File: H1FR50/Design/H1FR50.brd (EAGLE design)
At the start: 34.6 x 30 mm, 49 parts, among them P1 HEXABIT_17.32_NO_P6, U1 STM32F091CBU6, U2 TPS22943DCKR, U3 BGA824N6, U4 TESEO-LIV3F, U5 B39162B4327P810, X1 XTALL_CSTCE8M00G52

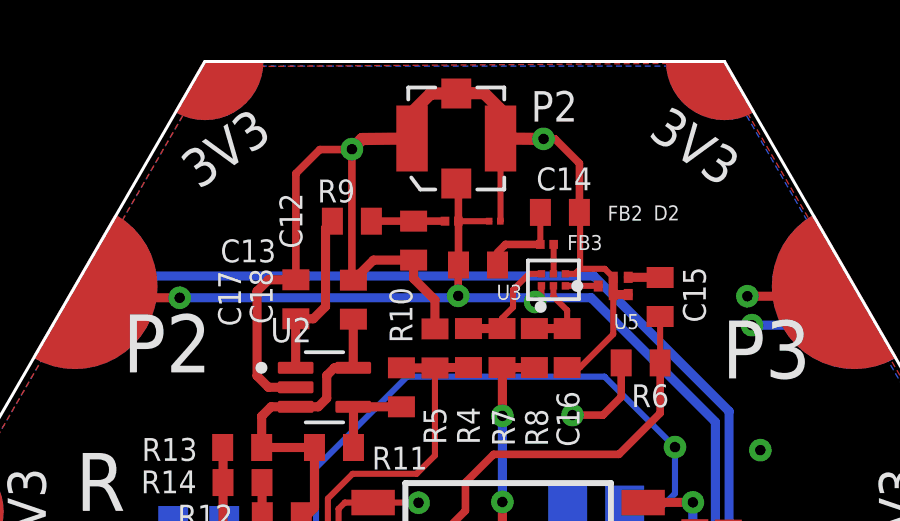
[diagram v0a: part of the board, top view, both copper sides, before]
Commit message: Added Keepout areas in PCB..
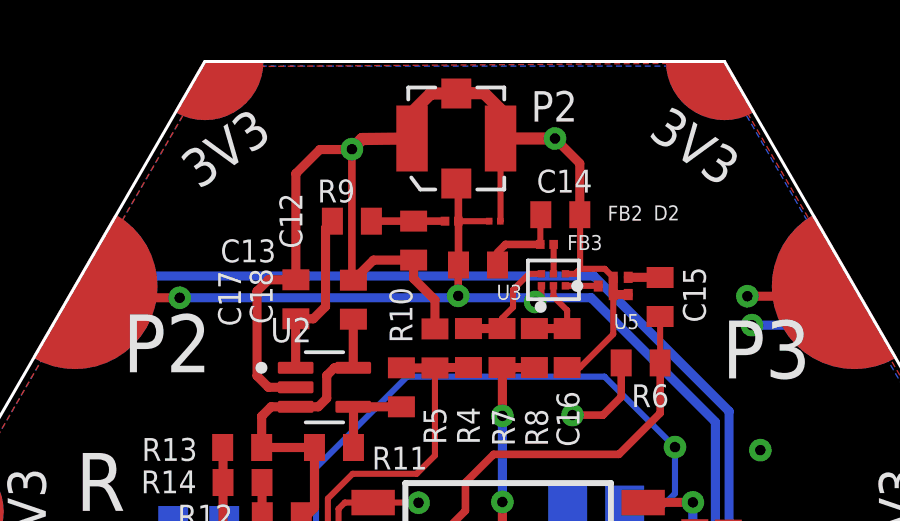
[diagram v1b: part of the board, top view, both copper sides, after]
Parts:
- moved C14 0.08 mm to (3.19, 9.89)
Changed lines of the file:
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@@
 <drawing>
 <settings>
-<setting alwaysvectorfont="no"/>
+<setting alwaysvectorfont="yes"/>
 <setting verticaltext="up"/>
 </settings>
@@
 <layer number="132" name="bAdjust" color="7" fill="1" visible="yes" active="yes"/>
 <layer number="133" name="bottom_silk" color="7" fill="1" visible="yes" active="yes"/>
+<layer number="134" name="cKeepout" color="16" fill="10" visible="yes" active="yes"/>
+<layer number="135" name="dKeepout" color="23" fill="10" visible="yes" active="yes"/>
 <layer number="144" name="Drill_legend" color="7" fill="1" visible="yes" active="yes"/>
 <layer number="145" name="DrillLegend_01-02" color="7" fill="1" visible="yes" active="yes"/>
@@
 <rectangle x1="-6.37920625" y1="-6.89889375" x2="-6.29081875" y2="-6.8841625" layer="21" rot="R180"/>
 <text x="3.6957" y="-12.5984" size="1.778" layer="25">D</text>
+<rectangle x1="-2.7178" y1="10.414" x2="2.3241" y2="14.6685" layer="39"/>
+<rectangle x1="-2.7178" y1="10.414" x2="2.3241" y2="14.6685" layer="40"/>
+<rectangle x1="-2.7178" y1="10.414" x2="2.3241" y2="14.6685" layer="135"/>
+<rectangle x1="-2.7178" y1="10.414" x2="2.3241" y2="14.6685" layer="134"/>
 </plain>
 <attributes>
@@
 <attribute name="VOLTAGE_RATING" value="" x="-21.2598" y="6.8199" size="1.778" layer="27" display="off"/>
 </element>
-<element name="C14" library="HEXABITZ_RCLS" library_urn="urn:adsk.eagle:library:20064561" package="C-0402" package3d_urn="urn:adsk.eagle:package:19666459/2" value="3.9pF" x="3.175" y="9.9695" smashed="yes" rot="R180">
-<attribute name="CAPACITANCE" value="" x="35.5727" y="15.8877" size="1.778" layer="27" rot="R180" display="off"/>
-<attribute name="MFN" value="" x="35.5727" y="15.8877" size="1.778" layer="27" rot="R180" display="off"/>
-<attribute name="MPN" value="" x="35.5727" y="15.8877" size="1.778" layer="27" rot="R180" display="off"/>
-<attribute name="NAME" x="2.3876" y="10.7061" size="0.762" layer="25"/>
-<attribute name="OCTOPART_URL" value="" x="35.5727" y="15.8877" size="1.778" layer="27" rot="R180" display="off"/>
-<attribute name="TOLERANCE" value="" x="35.5727" y="15.8877" size="1.778" layer="27" rot="R180" display="off"/>
-<attribute name="VALUE" x="3.81" y="11.8745" size="1.016" layer="27" rot="R180"/>
-<attribute name="VOLTAGE_RATING" value="" x="35.5727" y="15.8877" size="1.778" layer="27" rot="R180" display="off"/>
+<element name="C14" library="HEXABITZ_RCLS" library_urn="urn:adsk.eagle:library:20064561" package="C-0402" package3d_urn="urn:adsk.eagle:package:19666459/2" value="3.9pF" x="3.1877" y="9.8933" smashed="yes" rot="R180">
+<attribute name="CAPACITANCE" value="" x="35.5854" y="15.8115" size="1.778" layer="27" rot="R180" display="off"/>
+<attribute name="MFN" value="" x="35.5854" y="15.8115" size="1.778" layer="27" rot="R180" display="off"/>
+<attribute name="MPN" value="" x="35.5854" y="15.8115" size="1.778" layer="27" rot="R180" display="off"/>
+<attribute name="NAME" x="2.4003" y="10.6299" size="0.762" layer="25"/>
+<attribute name="OCTOPART_URL" value="" x="35.5854" y="15.8115" size="1.778" layer="27" rot="R180" display="off"/>
+<attribute name="TOLERANCE" value="" x="35.5854" y="15.8115" size="1.778" layer="27" rot="R180" display="off"/>
+<attribute name="VALUE" x="3.8227" y="11.7983" size="1.016" layer="27" rot="R180"/>
+<attribute name="VOLTAGE_RATING" value="" x="35.5854" y="15.8115" size="1.778" layer="27" rot="R180" display="off"/>
 </element>
 <element name="FB3" library="HEXABITZ_RCLS" library_urn="urn:adsk.eagle:library:20064561" package="FB-0402" package3d_urn="urn:adsk.eagle:package:27264799/1" value="6.8nH" x="2.7432" y="8.9027" smashed="yes">
@@
 <wire x1="-3.7592" y1="12.0777" x2="-3.420453125" y2="12.416446875" width="0.4064" layer="1"/>
 <via x="-3.7592" y="12.0777" extent="1-2" drill="0.35"/>
-<wire x1="2.6289" y1="12.4206" x2="2.62711875" y2="12.41881875" width="0.3048" layer="1"/>
-<wire x1="2.62711875" y1="12.41881875" x2="1.1956" y2="12.4333" width="0.4064" layer="1"/>
-<via x="2.6289" y="12.4206" extent="1-2" drill="0.35"/>
+<via x="3.0099" y="12.4333" extent="1-2" drill="0.35"/>
 <wire x1="3.3591" y1="7.9216" x2="3.6798" y2="7.9216" width="0.2032" layer="1"/>
 <wire x1="3.6798" y1="7.9216" x2="3.8481" y2="8.0899" width="0.2032" layer="1"/>
-<wire x1="3.8481" y1="8.0899" x2="3.8481" y2="9.9464" width="0.2032" layer="1"/>
-<wire x1="3.8481" y1="9.9464" x2="3.825" y2="9.9695" width="0.3048" layer="1"/>
+<wire x1="3.8481" y1="8.0899" x2="3.8481" y2="9.8829" width="0.2032" layer="1"/>
+<wire x1="3.8481" y1="9.8829" x2="3.8377" y2="9.8933" width="0.3048" layer="1"/>
 <wire x1="2.5591" y1="7.5216" x2="2.5591" y2="7.1946" width="0.2032" layer="1"/>
 <wire x1="2.5591" y1="7.1946" x2="2.3495" y2="6.985" width="0.2032" layer="1"/>
@@
 <wire x1="-2.3262" y1="-11.0638" x2="-2.7051" y2="-11.4427" width="0.2032" layer="16"/>
 <wire x1="-2.3262" y1="-11.0638" x2="-2.3262" y2="-10.51120625" width="0.2032" layer="16"/>
-<wire x1="3.825" y1="9.9695" x2="3.825" y2="11.6055" width="0.254" layer="1"/>
-<wire x1="3.825" y1="11.6055" x2="3.0099" y2="12.4206" width="0.254" layer="1"/>
-<wire x1="3.0099" y1="12.4206" x2="2.6289" y2="12.4206" width="0.254" layer="1"/>
-<wire x1="-5.6261" y1="7.7239" x2="-5.6261" y2="11.2649" width="0.254" layer="1"/>
-<wire x1="-4.826" y1="12.065" x2="-3.7592" y2="12.065" width="0.254" layer="1"/>
-<wire x1="-5.6261" y1="11.2649" x2="-4.826" y2="12.065" width="0.254" layer="1"/>
+<wire x1="3.8377" y1="9.8933" x2="3.8377" y2="11.5928" width="0.3048" layer="1"/>
+<wire x1="-5.6261" y1="7.7239" x2="-5.6261" y2="11.2649" width="0.3048" layer="1"/>
+<wire x1="-4.826" y1="12.065" x2="-3.7592" y2="12.065" width="0.3048" layer="1"/>
+<wire x1="-5.6261" y1="11.2649" x2="-4.826" y2="12.065" width="0.3048" layer="1"/>
 <wire x1="-3.8236" y1="-11.2513" x2="-4.7235" y2="-10.3514" width="0.2032" layer="1"/>
 <wire x1="-4.7235" y1="-10.3514" x2="-5.1435" y2="-10.3514" width="0.2032" layer="1"/>
@@
 <wire x1="-1.5425" y1="0.2979" x2="-1.5367" y2="0.2921" width="0.2032" layer="1"/>
 <via x="-1.5367" y="0.2921" extent="1-2" drill="0.35"/>
+<wire x1="1.1956" y1="12.4333" x2="3.0099" y2="12.4333" width="0.4064" layer="1"/>
+<wire x1="3.8377" y1="11.5928" x2="3.8377" y2="11.6055" width="0.2032" layer="1"/>
+<wire x1="3.8377" y1="11.6055" x2="3.0099" y2="12.4333" width="0.3048" layer="1"/>
 </signal>
 <signal name="VDD">
@@
 <contactref element="FB3" pad="1"/>
 <contactref element="C14" pad="2"/>
-<wire x1="2.5212" y1="9.9657" x2="2.525" y2="9.9695" width="0.3048" layer="1"/>
+<wire x1="2.5212" y1="9.8768" x2="2.5377" y2="9.8933" width="0.3048" layer="1"/>
 <wire x1="2.5212" y1="8.9027" x2="1.3612" y2="8.9027" width="0.254" layer="1"/>
 <wire x1="1.3612" y1="8.9027" x2="1.0945" y2="8.636" width="0.254" layer="1"/>
 <wire x1="1.0945" y1="8.636" x2="1.0945" y2="8.2169" width="0.2032" layer="1"/>
-<wire x1="2.5212" y1="8.9027" x2="2.5212" y2="9.9657" width="0.2032" layer="1"/>
+<wire x1="2.5212" y1="8.9027" x2="2.5212" y2="9.8768" width="0.2032" layer="1"/>
 </signal>
 <signal name="N$12">

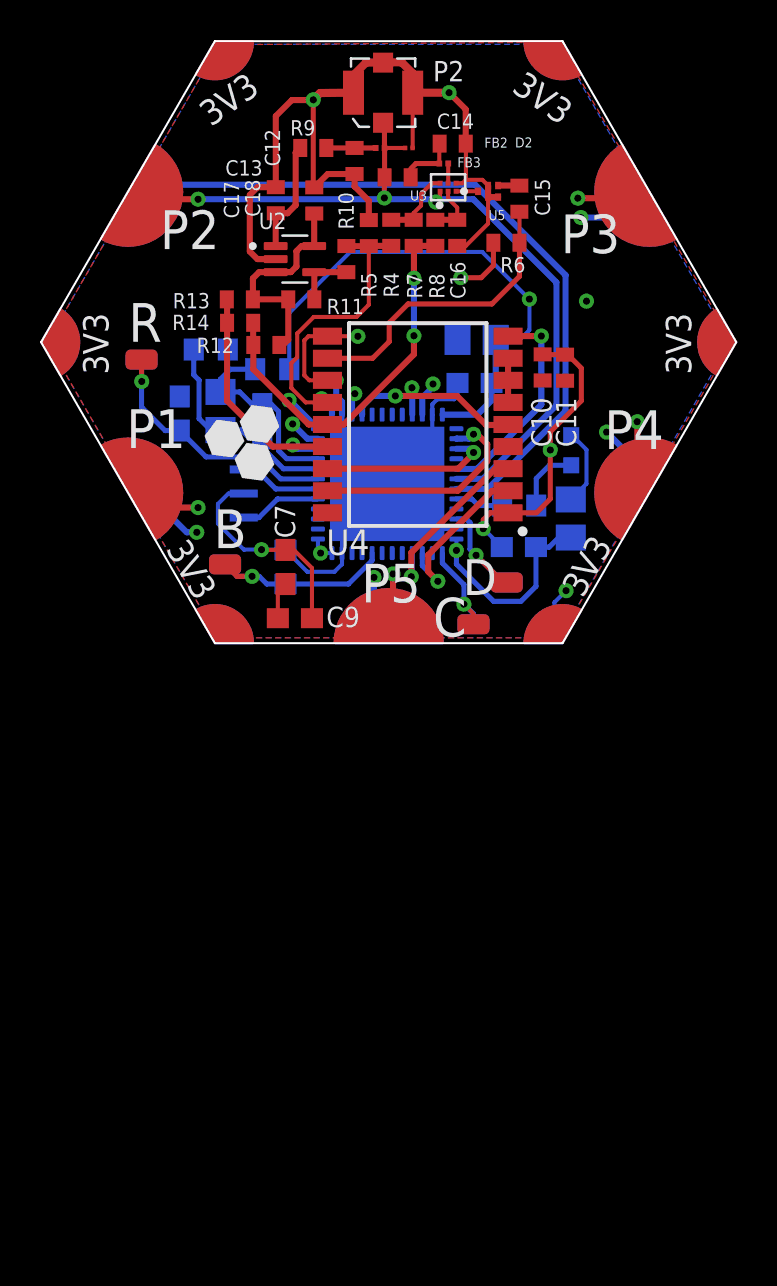
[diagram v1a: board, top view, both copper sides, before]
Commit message: - Rearanged all P#.. - Removed Keepout areas.. - Renamed all NM to DNP.. - Moved D1 from layer 16 to layer 1.. - Changed R8 from 0R NM to 0R.. - Placed more Grounding vias around RF connector in brd.. - Added two pullups res on I2C lines.. - Added the recomended filters on Tevo's power pins.. - Updated Document.. - Updated BOM..
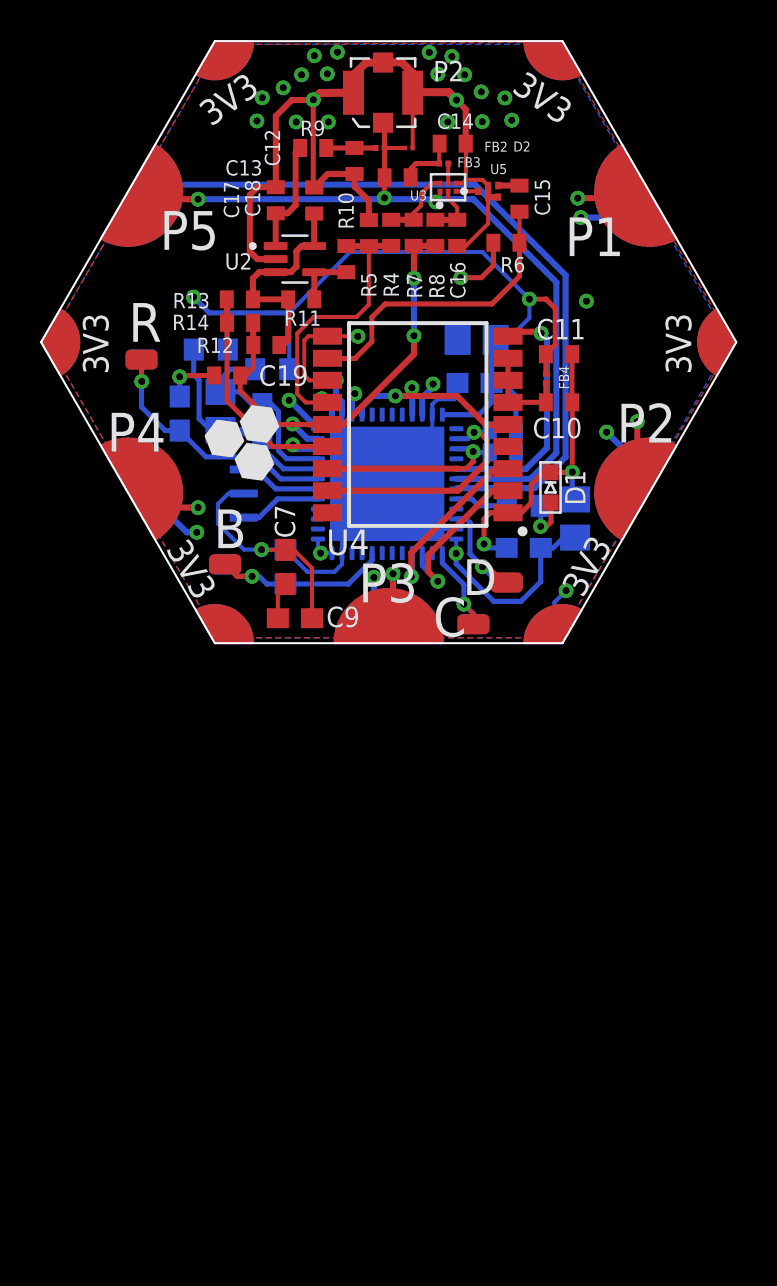
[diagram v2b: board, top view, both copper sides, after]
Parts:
- added C19: 56pF, HEXABITZ_RCLS:C-0402
- added FB4: 27nH, HEXABITZ_RCLS:FB-0402
- added R15, R16: 2.2k, HEXABITZ_RCLS:R-0402
- C10: value 100pF -> 56pF
- C11: value 100nF -> 10nF
- R11, R13, R6, R7, R9: value 0.0R NM -> DNP
- R14: value 3R NM -> DNP
- R8: value 0.0R NM -> 0.0R
- moved D1 2.12 mm to (8.06, -7.24), flipped to the top
- moved C10 1.92 mm to (8.48, -3.00), turned to 180 degrees
- moved C11 0.74 mm to (8.48, -0.60), turned to 180 degrees
- moved C6 0.24 mm to (6.73, -10.2)
- moved R1 0.23 mm to (6.73, -8.15)
- moved C3 0.22 mm to (9.29, -8.79)
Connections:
- new net VCC_RF1: C10.2, FB4.1, U4.6, U4.7, U4.8
- net GND: now also C10.1, C11.1, C19.1; no longer C10.2, C11.2
- net I2C_CLOCK: now also R15.2
- net I2C_DATA: now also R16.2
- net VCC_RF: now also C19.2
- net VDD: now also C11.2, FB4.2, R15.1, R16.1; no longer C10.1, C11.1, U4.6, U4.7, U4.8
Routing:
- net VDD: track 41.8 -> 53.7 mm, vias 3 -> 4
- net VCC_RF1: track 0.00 -> 5.06 mm
- net SYS_RESET: track 10.6 -> 12.6 mm
- net VCC_RF: track 19.4 -> 21.1 mm
- net USART1_TX: track 35.1 -> 36.5 mm
- net USART1_RX: track 37.2 -> 38.5 mm
- net I2C_DATA: track 8.57 -> 9.64 mm
- net I2C_CLOCK: track 11.3 -> 12.3 mm
- net N$10: track 3.36 -> 2.64 mm, vias 0 -> 1
- net GND: track 103.5 -> 103.2 mm, vias 8 -> 9

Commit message: - Redesigned both Schematic and PCB.. - Updated BOM and Documentation..
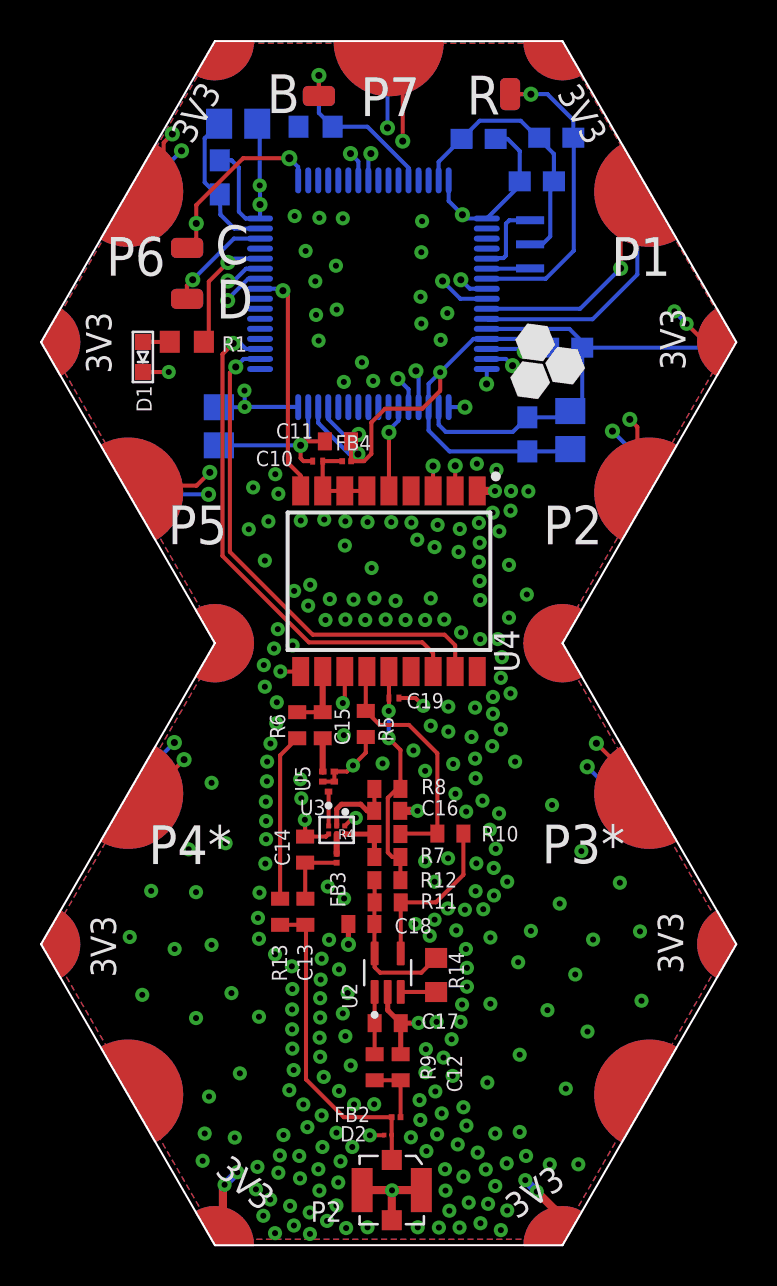
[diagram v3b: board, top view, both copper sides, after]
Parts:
- removed FB1: FB-TDK_MMZ1608Y300B, Hexabitz:FB-TDK_MMZ1608Y300B
- removed R15, R16: 2.2k, HEXABITZ_RCLS:R-0402
- removed R3: 0.0R, Hexabitz:R-0603
- C1: value 100nF -> 10nF
- C10, C19: device HEXABITZ_RCLS:C-0402 -> HEXABITZ_RCLS:C-0201
- C17: value 1uF -> 1.00uF
- C3: value 4.7uF -> 100nF; device Hexabitz:C-0805-POL -> Hexabitz:C-0603
- C5: value 10nF -> 100nF
- C7: value 100nF -> 4.7uF; device Hexabitz:C-0603 -> Hexabitz:C-0805-POL
- P1: value HEXABIT_17.32_NO_P6 -> HEXABIT_17.32_X2_NO_P5; device hexabitz_connectors:HEXABIT_17.32_NO_P6 -> hexabitz_connectors:HEXABIT_17.32_X2_NO_P5
- R14: value DNP -> 100k; device HEXABITZ_RCLS:R-0402 -> HEXABITZ_RCLS:R-0603
- U1: value STM32F091CBU6 -> STM32F091RBT6STMICROELECTRONICS_STM32F091RBT6_0_1; device Hexabitz:STM32F091CBU6 -> Hexabitz:STMICROELECTRONICS_STM32F091RBT6_1
- moved P2 54.7 mm to (0.15, -42.3), turned to 180 degrees
- moved D2 49.2 mm to (-0.04, -39.5), turned to 0 degrees
- moved FB2 48.3 mm to (0.37, -38.6), turned to 180 degrees
- moved R9 45.9 mm to (-0.70, -36.1), turned to 270 degrees
- moved C12 45.2 mm to (0.60, -36.1), turned to 270 degrees
- moved C17 41.4 mm to (-0.05, -33.9), turned to 0 degrees
- moved C13 36.9 mm to (-4.15, -28.4), turned to 90 degrees
- moved C18 36.1 mm to (-1.36, -29.0), turned to 180 degrees
- moved C14 35.9 mm to (-4.17, -25.3), turned to 270 degrees
- moved U2 35.9 mm to (-0.05, -31.4), turned to 90 degrees
- moved FB3 35.0 mm to (-2.59, -25.7), turned to 90 degrees
- moved R14 33.9 mm to (2.36, -31.5), turned to 270 degrees
- moved U3 32.5 mm to (-2.59, -24.3), turned to 270 degrees
- moved R7 31.1 mm to (-0.06, -25.7), turned to 0 degrees
- moved R13 30.6 mm to (-5.41, -28.4), turned to 270 degrees
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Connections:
- removed net USART1_RX: P1.PAD_PD5, U1.P$31
- removed net USART1_TX: P1.PAD_PU5, U1.P$30
- removed net USART2_RX: P1.PAD_PD2, U1.P$13
- removed net USART2_TX: P1.PAD_PU2, U1.P$12
- removed net USART3_RX: P1.PAD_PD4, U1.P$22
- removed net USART3_TX: P1.PAD_PU4, U1.P$21
- removed net USART4_RX: P1.PAD_PD1, U1.P$11
- removed net USART4_TX: P1.PAD_PU1, U1.P$10
- removed net USART5_RX: U1.P$40, U4.3
- removed net USART5_TX: U1.P$39, U4.2
- removed net USART6_RX: P1.PAD_PD3, U1.P$15
- removed net USART6_TX: P1.PAD_PU3, U1.P$14
- removed net VANT: R13.1, R14.1, U4.15
- removed net VDDA: C2.1, C5.1, FB1.1, U1.P$9
- removed net VSSA: C2.2, C5.2, R3.2, U1.P$8
- new net GND3: P1.PAD_PD13
- new net GND8: P1.PAD_PD18
- new net N$10: R1.2, U1.44
- new net N$3: C13.1, D2.2, FB2.2, P2.1, R13.2
- new net UART1_RX*: P1.PAD_PD7, U1.43
- new net UART1_TX*: P1.PAD_PU7, U1.42
- new net UART2_RX*: P1.PAD_PD3, U1.17
- new net UART2_TX*: P1.PAD_PU3, U1.16
- new net UART3_RX: U1.30, U4.3
- new net UART3_TX: U1.29, U4.2
- new net UART4_RX: P1.PAD_PD2, U1.15
- new net UART4_TX: P1.PAD_PU2, U1.14
- new net UART5_RX: P1.PAD_PD8, U1.56
- new net UART5_TX: P1.PAD_PU8, U1.55
- new net UART6_RX: P1.PAD_PD10, U1.21
- new net UART6_TX: P1.PAD_PU10, U1.20
- new net UART7_RX: P1.PAD_PD9, U1.9
- new net UART7_TX: P1.PAD_PU9, U1.8
- new net UART8_RX: P1.PAD_PD1, U1.11
- new net UART8_TX: P1.PAD_PU1, U1.10
- new net VDD3: P1.PAD_PU13
- new net VDD8: P1.PAD_PU18
- net ANT_IN: now also R13.1; no longer C13.1, D2.2, FB2.2, P2.1
- net B1: now also U1.60; no longer U1.P$44
- net GND: now also C2.2, C5.2, P1.PAD_PD14, P1.PAD_PD15, P1.PAD_PD16, P1.PAD_PD17, P1.PAD_PD19, P1.PAD_PD20, U1.12, U1.18, U1.31, U1.47, U1.63; no longer P1.PAD_PD10, P1.PAD_PD7, P1.PAD_PD8, P1.PAD_PD9, R3.1, U1.EP, U1.P$23, U1.P$35, U1.P$47
- net I2C_CLOCK: now also U1.34; no longer R15.2, U1.P$26
- net I2C_DATA: now also U1.35; no longer R16.2, U1.P$27
- net N$2: now also R14.2, U2.3; no longer R1.2, U1.P$32
- net N$23: now also R14.1; no longer R13.2, U2.3
- net N$5: now also U1.5; no longer U1.P$5
- net N$6: now also U1.6; no longer U1.P$6
- net N$7: now also U1.46; no longer U1.P$34
- net N$9: now also U1.49; no longer U1.P$37
- net R1: now also C8.1, U1.7; no longer C1.1, U1.P$7
- net SYS_RESET: now also U1.41; no longer U1.P$29
- net SYS_WAKEUP: now also U1.22; no longer U1.P$16
- net VCC_RF: no longer R14.2
- net VDD: now also C1.1, C2.1, C5.1, P1.PAD_PU14, P1.PAD_PU15, P1.PAD_PU16, P1.PAD_PU17, P1.PAD_PU19, P1.PAD_PU20, U1.1, U1.13, U1.19, U1.32, U1.48, U1.64; no longer C8.1, FB1.2, P1.PAD_PU10, P1.PAD_PU7, P1.PAD_PU8, P1.PAD_PU9, R15.1, R16.1, U1.P$1, U1.P$24, U1.P$36, U1.P$48
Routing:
- net USART1_RX: track 38.5 -> 0.00 mm
- net USART1_TX: track 36.5 -> 0.00 mm, vias 1 -> 0
- net UART1_RX*: track 0.00 -> 31.7 mm, vias 0 -> 2
- net UART1_TX*: track 0.00 -> 30.7 mm, vias 0 -> 2
- net USART4_TX: track 29.0 -> 0.00 mm, vias 2 -> 0
- net USART2_TX: track 28.0 -> 0.00 mm, vias 2 -> 0
- net UART7_TX: track 0.00 -> 27.0 mm, vias 0 -> 2
- net USART4_RX: track 26.7 -> 0.00 mm, vias 2 -> 0
- net UART7_RX: track 0.00 -> 26.5 mm, vias 0 -> 2
- net UART5_RX: track 0.00 -> 25.3 mm, vias 0 -> 2
- net UART2_TX*: track 0.00 -> 24.6 mm, vias 0 -> 2
- net UART2_RX*: track 0.00 -> 24.5 mm, vias 0 -> 2
- net GND: track 103.2 -> 78.7 mm, vias 9 -> 274
- net UART5_TX: track 0.00 -> 24.4 mm, vias 0 -> 2
- net USART6_TX: track 23.2 -> 0.00 mm, vias 2 -> 0
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- added copper zone on layer 15, net VDD
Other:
- board size 34.6 x 30 mm -> 34.6 x 60 mm
- board text added: "P3*"
- board text added: "P4*"
- board text added: "P6"
- board text added: "P7"
- board text removed: "P3"
- board text removed: "P4"
